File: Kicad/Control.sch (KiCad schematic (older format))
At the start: 8 parts, among them U17 74HCT574, U18 74HCT161, U19 74HCT138, U20 74HCT151, U21 74HCT139, U22 74HCT154, U25 AT27C1024-70PU, U4 74HCT240

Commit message: Added the equ pseudo-op. Rearranged the PCB layout.
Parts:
- U18, U19, U20, U21: footprint Package_SO:SOIC-16W_5.3x10.2mm_P1.27mm -> Package_SO:SOIC-16_3.9x9.9mm_P1.27mm
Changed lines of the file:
@@
 F 0 "U18" H 1700 5500 50  0000 C CNN
 F 1 "74HCT161" H 1650 5400 50  0000 C CNN
-F 2 "Package_SO:SOIC-16W_5.3x10.2mm_P1.27mm" H 1850 4600 50  0001 C CNN
+F 2 "Package_SO:SOIC-16_3.9x9.9mm_P1.27mm" H 1850 4600 50  0001 C CNN
 F 3 "http://www.ti.com/lit/gpn/sn74LS161" H 1850 4600 50  0001 C CNN
 F 4 "uSeq Counter" H 1850 4600 50  0001 C CNN "Description"
@@
 F 0 "U20" H 7250 2666 50  0000 C CNN
 F 1 "74HCT151" H 7250 2575 50  0000 C CNN
-F 2 "Package_SO:SOIC-16W_5.3x10.2mm_P1.27mm" H 7250 1800 50  0001 C CNN
+F 2 "Package_SO:SOIC-16_3.9x9.9mm_P1.27mm" H 7250 1800 50  0001 C CNN
 F 3 "" H 7250 1800 50  0001 C CNN
 F 4 "Jump Logic" H 7250 1800 50  0001 C CNN "Description"
@@
 F 0 "U19" H 9400 3250 50  0000 C CNN
 F 1 "74HCT138" H 9400 3150 50  0000 C CNN
-F 2 "Package_SO:SOIC-16W_5.3x10.2mm_P1.27mm" H 9650 2550 50  0001 C CNN
+F 2 "Package_SO:SOIC-16_3.9x9.9mm_P1.27mm" H 9650 2550 50  0001 C CNN
 F 3 "http://www.ti.com/lit/gpn/sn74LS138" H 9650 2550 50  0001 C CNN
 F 4 "Databus Write Demux" H 9650 2550 50  0001 C CNN "Description"
@@
 F 0 "U21" H 7250 4467 50  0000 C CNN
 F 1 "74HCT139" H 7250 4376 50  0000 C CNN
-F 2 "Package_SO:SOIC-16W_5.3x10.2mm_P1.27mm" H 7250 4100 50  0001 C CNN
+F 2 "Package_SO:SOIC-16_3.9x9.9mm_P1.27mm" H 7250 4100 50  0001 C CNN
 F 3 "http://www.ti.com/lit/gpn/sn74LS139" H 7250 4100 50  0001 C CNN
 F 4 "PCincr and Address Write Demux" H 7250 4100 50  0001 C CNN "Description"
@@
 F 0 "U21" H 7250 3567 50  0000 C CNN
 F 1 "74HCT139" H 7250 3476 50  0000 C CNN
-F 2 "Package_SO:SOIC-16W_5.3x10.2mm_P1.27mm" H 7250 3200 50  0001 C CNN
+F 2 "Package_SO:SOIC-16_3.9x9.9mm_P1.27mm" H 7250 3200 50  0001 C CNN
 F 3 "http://www.ti.com/lit/gpn/sn74LS139" H 7250 3200 50  0001 C CNN
 F 4 "PCincr and Address Write Demux" H 7250 3200 50  0001 C CNN "Description"

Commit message: Lots of changes.
I found a few wiring mistakes in the schematic and fixed them up.
I added microcode instructions to allow B to be copied out to A,
to the UART and to memory. I added a lot of `mem = mem op B`
instructions. I added some examples to test the above. I redid the
PCB layout and added copper pours.
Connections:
- net Clk: no longer U21.1 (E), U21.15 (E)
- net Lo: now also U21.1 (E), U21.15 (E)
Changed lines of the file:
@@
 encoding utf-8
 Sheet 5 5
-Title ""
-Date ""
+Title "FISC TTL CPU"
+Date "2020-05-21"
 Rev ""
 Comp ""
@@
 Wire Wire Line
 	7750 4200 8000 4200
-Text GLabel 6550 4300 0    50   Input ~ 0
-Clk
 Wire Wire Line
 	6550 4300 6750 4300
@@
 	1    0    0    -1
 $EndComp
-Text GLabel 6500 3400 0    50   Input ~ 0
-Clk
 Text GLabel 6500 3100 0    50   Input ~ 0
 StkOp1
@@
 Wire Wire Line
 	3050 5600 2850 5600
-Text Notes 7350 3350 2    50   ~ 0
-PC\nIncrement
 Text Notes 3600 6300 2    50   ~ 0
 Databus\n Read\nDemux
@@
 Text Notes 10350 3050 0    50   ~ 0
 Outputs are high\nuntil Clk goes low
-Text Notes 6300 3700 0    50   ~ 0
-Outputs are high\nuntil Clk goes low
 Text Notes 2450 6150 0    50   ~ 0
 Outputs are high\nuntil Clk goes low
@@
 Text Notes 7000 5200 0    50   ~ 0
 The '240 is simply eight inverters to get the active level\nright for seven control lines. One other inverter creates the\ninverted clock signal.
+Text Notes 7350 3350 2    50   ~ 0
+PC\nIncrement
+Text GLabel 6550 4300 0    50   Input ~ 0
+Lo
 Wire Wire Line
 	2350 4400 2850 4400
@@
 Wire Bus Line
 	2950 1900 2950 4400
+Text GLabel 6500 3400 0    50   Input ~ 0
+Lo
 $EndSCHEMATC

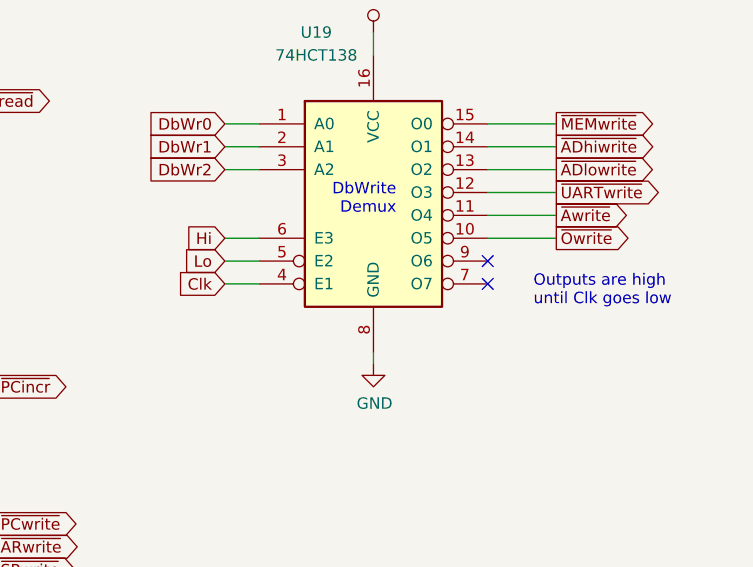
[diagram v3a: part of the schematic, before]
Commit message: Fixed up a bug in csim and a wiring error in the databus write demux.
Also, updated my journal with the build details to date.
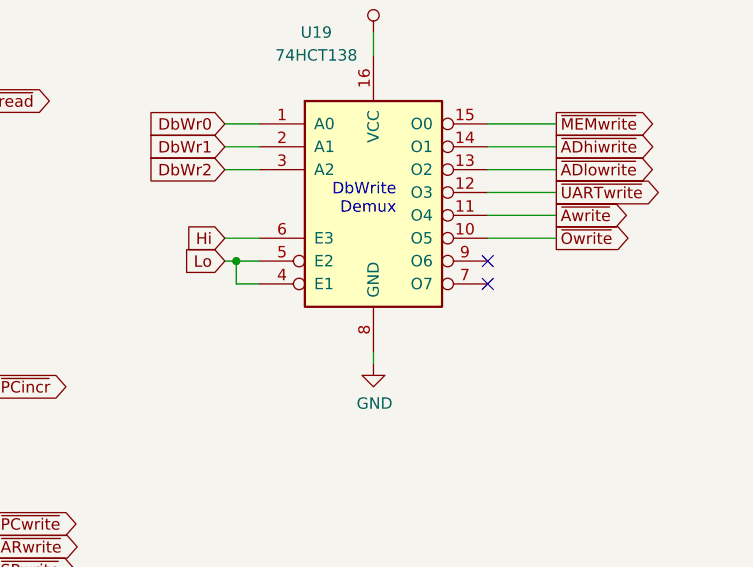
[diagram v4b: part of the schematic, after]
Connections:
- net Clk: no longer U19.4 (E1)
- net Lo: now also U19.4 (E1)
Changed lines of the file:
@@
 Text GLabel 9000 2850 0    50   Input ~ 0
 Lo
-Text GLabel 9000 2950 0    50   Input ~ 0
-Clk
 Wire Wire Line
 	9000 2750 9150 2750
 Wire Wire Line
-	9000 2850 9150 2850
-Wire Wire Line
-	9000 2950 9150 2950
+	9000 2850 9050 2850
 Text GLabel 10450 2350 2    50   Output ~ 0
 ~ADhiwrite
@@
 Wire Wire Line
 	4050 5600 5050 5600
-Text Notes 10350 3050 0    50   ~ 0
-Outputs are high\nuntil Clk goes low
 Text Notes 2450 6150 0    50   ~ 0
 Outputs are high\nuntil Clk goes low
@@
 Text GLabel 6550 4300 0    50   Input ~ 0
 Lo
-Wire Wire Line
-	2350 4400 2850 4400
-Wire Wire Line
-	2350 4100 2850 4100
-Wire Wire Line
-	2350 4200 2850 4200
-Wire Wire Line
-	2350 4300 2850 4300
+Text GLabel 6500 3400 0    50   Input ~ 0
+Lo
 Wire Bus Line
 	2750 3500 2750 4300
+Wire Wire Line
+	9150 2950 9050 2950
+Wire Wire Line
+	9050 2950 9050 2850
+Wire Wire Line
+	2350 4400 2850 4400
+Wire Wire Line
+	2350 4100 2850 4100
+Wire Wire Line
+	2350 4200 2850 4200
+Wire Wire Line
+	2350 4300 2850 4300
 Wire Bus Line
 	1050 750  1050 2400
 Wire Bus Line
 	2950 1900 2950 4400
-Text GLabel 6500 3400 0    50   Input ~ 0
-Lo
+Connection ~ 9050 2850
+Wire Wire Line
+	9050 2850 9150 2850
 $EndSCHEMATC
